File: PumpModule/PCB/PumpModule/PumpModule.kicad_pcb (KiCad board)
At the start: 2 copper layers, 55 x 105 mm, 12 parts, among them J5 Bus, J6 Motor, J7 Switch

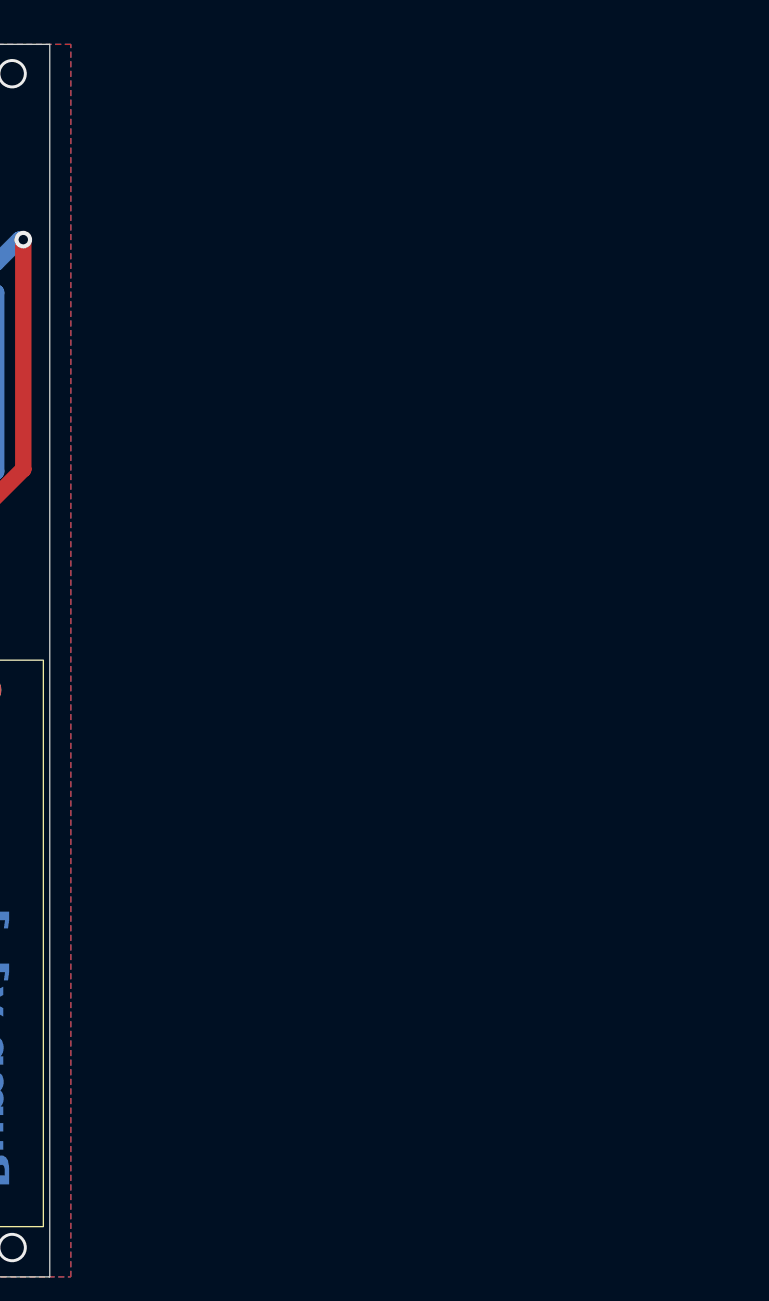
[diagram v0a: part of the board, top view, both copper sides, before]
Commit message: [PumpModule][PCB] Add Manufacturing files for 2 PumpModule v1.1 on board
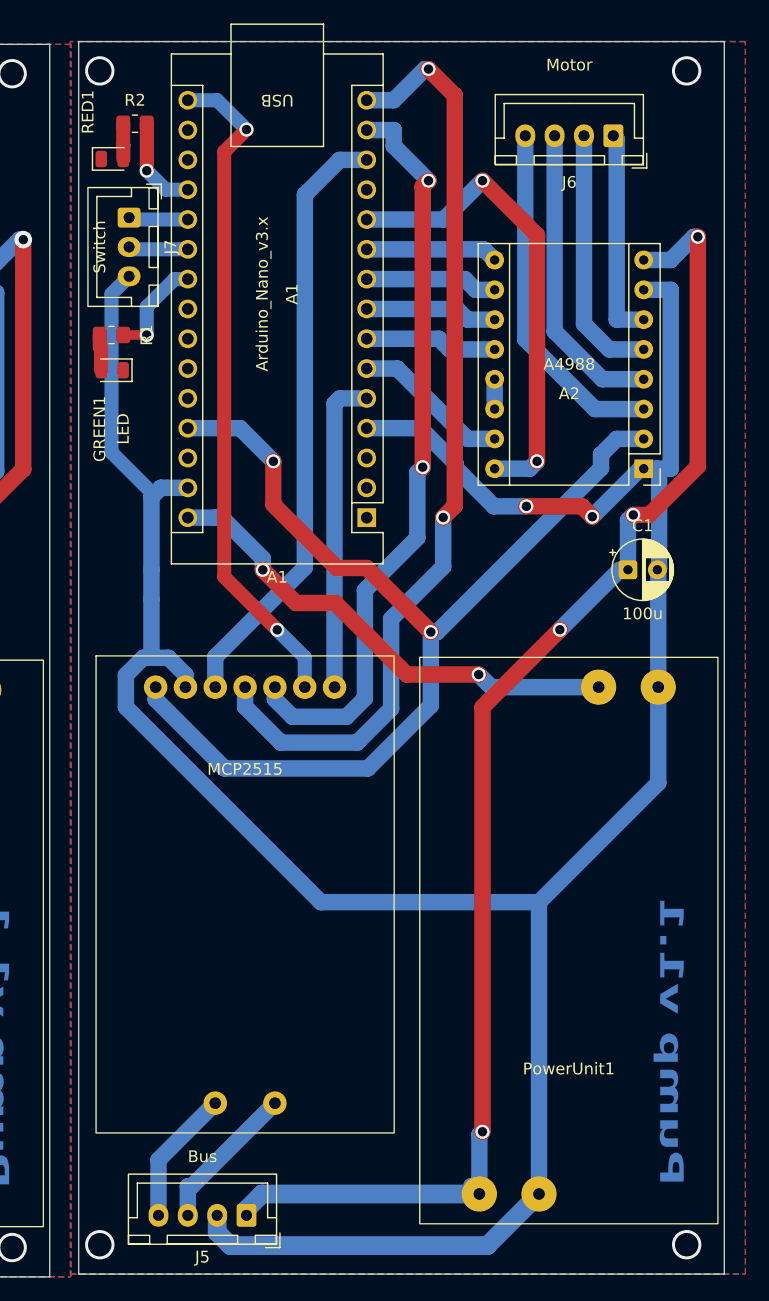
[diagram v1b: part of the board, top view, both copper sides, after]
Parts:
- added A1: Arduino_Nano_v3.x, Module:Arduino_Nano, F.Cu at (120.2, 70.3)
- added A2: A4988, Module:Pololu_Breakout-16_15.2x20.3mm, F.Cu at (143.8, 66.2)
- added C1: 100u, Capacitor_THT:CP_Radial_D5.0mm_P2.50mm, F.Cu at (142.5, 74.8)
- added GREEN1: LED, LED_SMD:LED_0805_2012Metric, F.Cu at (98.5, 57.8)
- added J5: Bus, Connector_JST:JST_XH_B4B-XH-A_1x04_P2.50mm_Vertical, F.Cu at (110.0, 129.8)
- added J6: Motor, Connector_JST:JST_XH_B4B-XH-A_1x04_P2.50mm_Vertical, F.Cu at (141.2, 37.8)
- added J7: Switch, Connector_JST:JST_XH_B3B-XH-A_1x03_P2.50mm_Vertical, F.Cu at (100.0, 44.8)
- added MCP2515: ~, PumpModule:MCP2515Mudule, F.Cu at (109.8, 92.3)
- added PowerUnit1: ~, PumpModule:DC-DC_Low, F.Cu at (137.4, 117.8)
- added R1: R, Resistor_SMD:R_0805_2012Metric_Pad1.20x1.40mm_HandSolder, F.Cu at (98.5, 54.8)
- added R2: R, Resistor_SMD:R_0805_2012Metric_Pad1.20x1.40mm_HandSolder, F.Cu at (100.5, 36.8)
- added RED1: LED, LED_SMD:LED_0805_2012Metric, F.Cu at (98.5, 39.8)
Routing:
- net GND: track 235.9 -> 471.8 mm, vias 2 -> 4
- net +12V: track 117.7 -> 235.5 mm, vias 4 -> 8
- net +5V: track 91.1 -> 182.2 mm, vias 2 -> 4
- net Net-(A1-D12): track 80.6 -> 161.2 mm, vias 2 -> 4
- net Net-(A1-D11): track 64.1 -> 128.3 mm, vias 2 -> 4
- net Net-(A1-D13): track 57.2 -> 114.3 mm, vias 2 -> 4
- net Net-(A1-D10): track 51.6 -> 103.2 mm
- net Net-(A1-VIN): track 41.5 -> 83.1 mm, vias 2 -> 4
- net Net-(A1-D8): track 40.9 -> 81.9 mm, vias 2 -> 4
- net Net-(A2-1B): track 29.9 -> 59.8 mm
- net Net-(A1-D2): track 27.1 -> 54.2 mm
- net Net-(A2-1A): track 25.9 -> 51.9 mm
- net Net-(A2-2A): track 22.0 -> 44.1 mm
- net Net-(A2-2B): track 18.1 -> 36.2 mm
- net Net-(A1-D3): track 13.4 -> 26.8 mm
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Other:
- board size 55 x 105 mm -> 112.5 x 105.2 mm

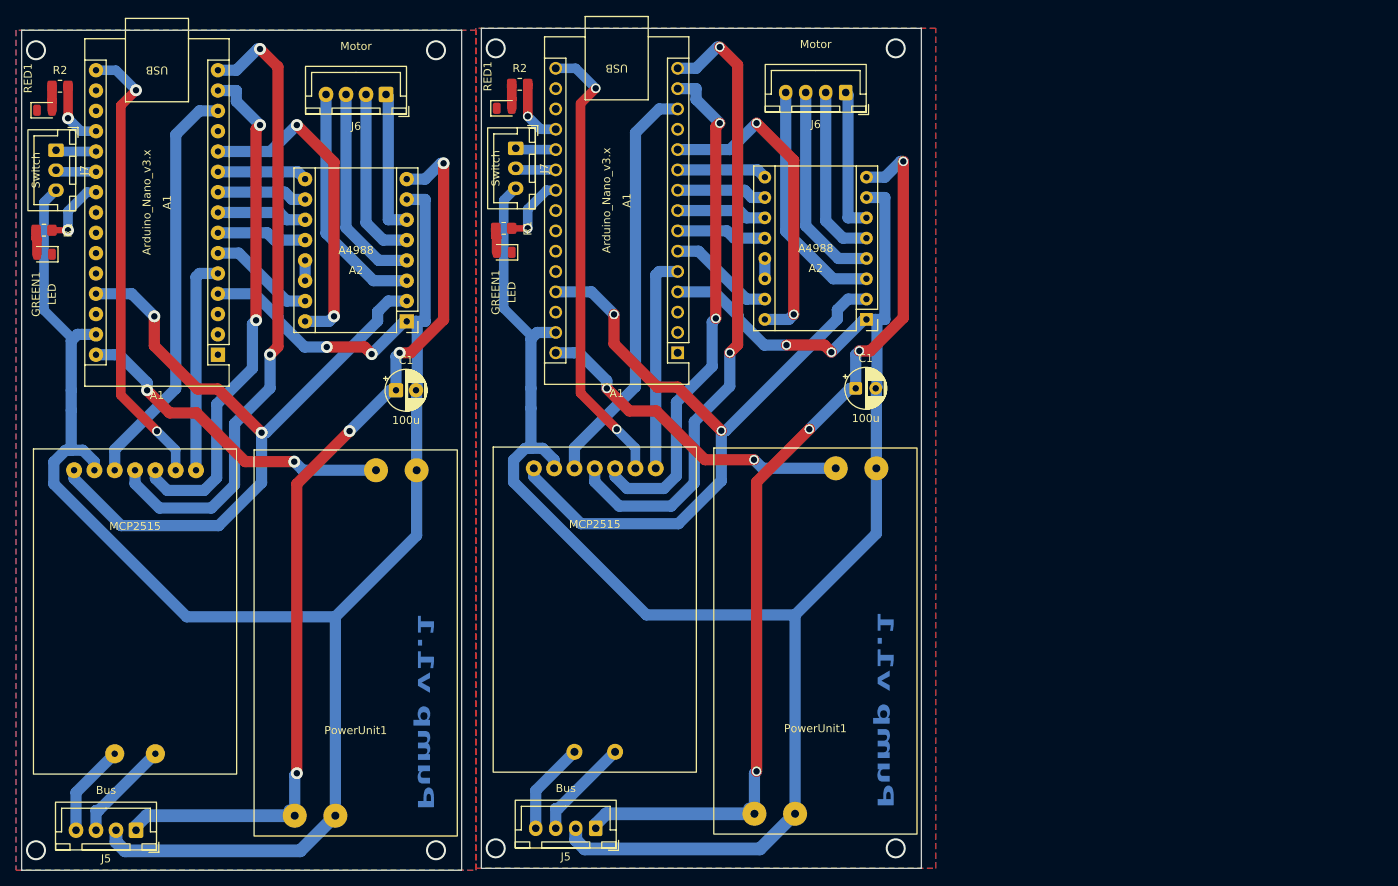
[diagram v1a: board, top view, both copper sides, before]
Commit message: [PumpModule][PCB] Fixed size of pins on PCB(v1.2)
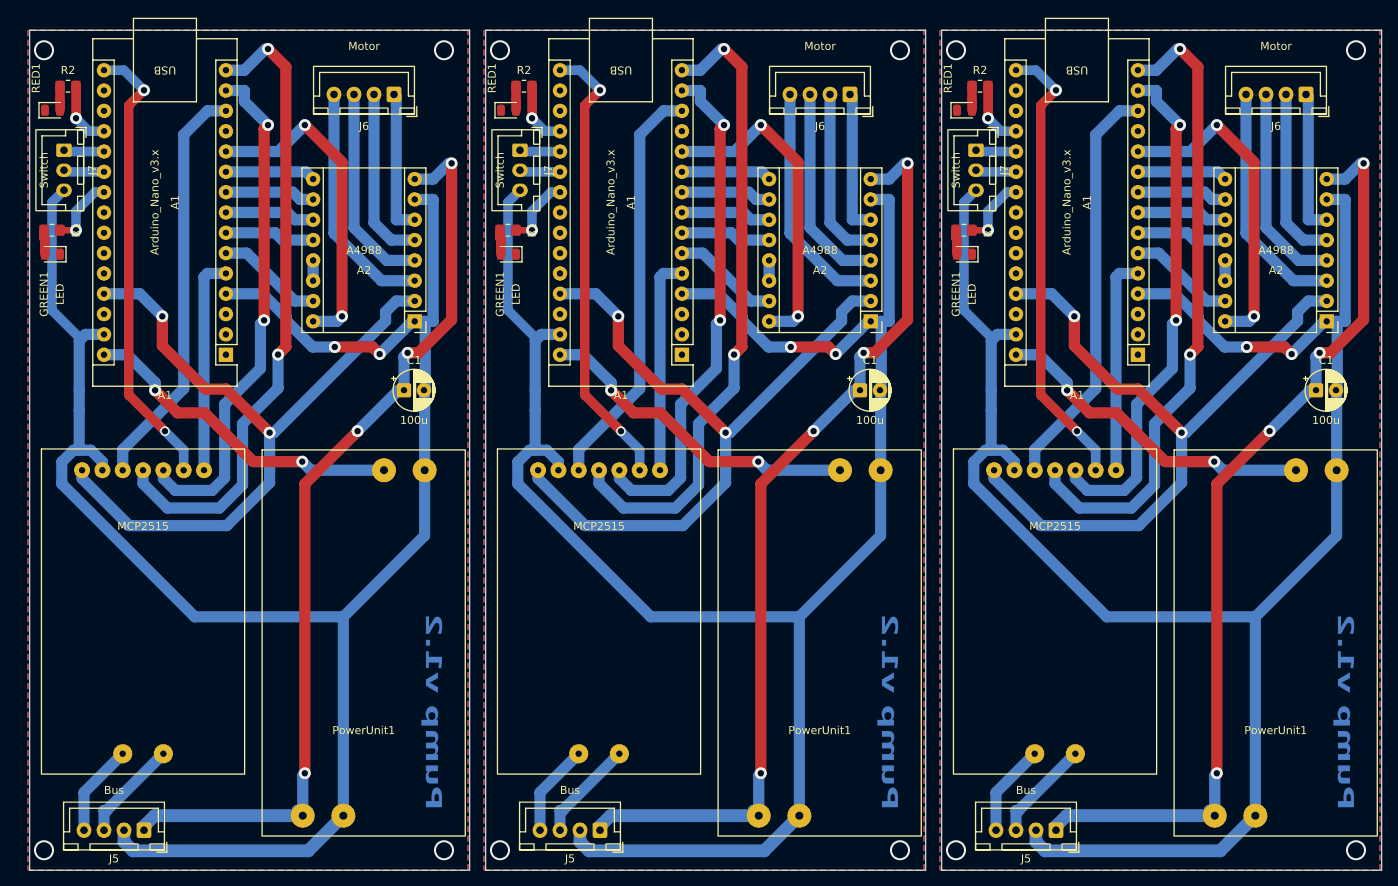
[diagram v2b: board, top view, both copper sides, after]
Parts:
- removed the A1 at (120.2, 70.3)
- removed the A2 at (143.8, 66.2)
- removed the C1 at (142.5, 74.8)
- removed the GREEN1 at (98.5, 57.8)
- removed the J5 at (110.0, 129.8)
- removed the J6 at (141.2, 37.8)
- removed the J7 at (100.0, 44.8)
- removed the MCP2515 at (109.8, 92.3)
- removed the PowerUnit1 at (137.4, 117.8)
- removed the R1 at (98.5, 54.8)
- removed the R2 at (100.5, 36.8)
- removed the RED1 at (98.5, 39.8)
- added A1: Arduino_Nano_v3.x, Module:Arduino_Nano, F.Cu at (177.7, 70.6)
- added A1: Arduino_Nano_v3.x, Module:Arduino_Nano, F.Cu at (120.7, 70.6)
- added A2: A4988, Module:Pololu_Breakout-16_15.2x20.3mm, F.Cu at (144.3, 66.4)
- added A2: A4988, Module:Pololu_Breakout-16_15.2x20.3mm, F.Cu at (201.3, 66.4)
- added C1: 100u, Capacitor_THT:CP_Radial_D5.0mm_P2.50mm, F.Cu at (200.0, 75.0)
- added C1: 100u, Capacitor_THT:CP_Radial_D5.0mm_P2.50mm, F.Cu at (143.0, 75.0)
- added GREEN1: LED, LED_SMD:LED_0805_2012Metric, F.Cu at (99.1, 58.0)
- added GREEN1: LED, LED_SMD:LED_0805_2012Metric, F.Cu at (156.1, 58.0)
- added J5: Bus, Connector_JST:JST_XH_B4B-XH-A_1x04_P2.50mm_Vertical, F.Cu at (110.5, 130.0)
- added J5: Bus, Connector_JST:JST_XH_B4B-XH-A_1x04_P2.50mm_Vertical, F.Cu at (167.5, 130.0)
- added J6: Motor, Connector_JST:JST_XH_B4B-XH-A_1x04_P2.50mm_Vertical, F.Cu at (198.8, 38.0)
- added J6: Motor, Connector_JST:JST_XH_B4B-XH-A_1x04_P2.50mm_Vertical, F.Cu at (141.8, 38.0)
- added J7: Switch, Connector_JST:JST_XH_B3B-XH-A_1x03_P2.50mm_Vertical, F.Cu at (157.5, 45.0)
- added J7: Switch, Connector_JST:JST_XH_B3B-XH-A_1x03_P2.50mm_Vertical, F.Cu at (100.5, 45.0)
- added MCP2515: ~, PumpModule:MCP2515Mudule, F.Cu at (110.4, 92.5)
- added MCP2515: ~, PumpModule:MCP2515Mudule, F.Cu at (167.4, 92.5)
- added PowerUnit1: ~, PumpModule:DC-DC_Low, F.Cu at (138.0, 118.0)
- added PowerUnit1: ~, PumpModule:DC-DC_Low, F.Cu at (195.0, 118.0)
- added R1: R, Resistor_SMD:R_0805_2012Metric_Pad1.20x1.40mm_HandSolder, F.Cu at (99.0, 55.0)
- added R1: R, Resistor_SMD:R_0805_2012Metric_Pad1.20x1.40mm_HandSolder, F.Cu at (156.0, 55.0)
- added R2: R, Resistor_SMD:R_0805_2012Metric_Pad1.20x1.40mm_HandSolder, F.Cu at (158.0, 37.0)
- added R2: R, Resistor_SMD:R_0805_2012Metric_Pad1.20x1.40mm_HandSolder, F.Cu at (101.0, 37.0)
- added RED1: LED, LED_SMD:LED_0805_2012Metric, F.Cu at (99.1, 40.0)
- added RED1: LED, LED_SMD:LED_0805_2012Metric, F.Cu at (156.1, 40.0)
- moved A1 1.00 mm to (63.7, 70.6)
- moved A2 1.00 mm to (87.3, 66.4)
- moved C1 1.00 mm to (86.0, 75.0)
- moved GREEN1 1.00 mm to (42.1, 58.0)
- moved J5 1.00 mm to (53.5, 130.0)
- moved J6 1.00 mm to (84.8, 38.0)
- moved J7 1.00 mm to (43.5, 45.0)
- moved MCP2515 1.00 mm to (53.4, 92.5)
- moved PowerUnit1 1.00 mm to (81.0, 118.0)
- moved R1 1.00 mm to (42.0, 55.0)
- moved R2 1.00 mm to (44.0, 37.0)
- moved RED1 1.00 mm to (42.1, 40.0)
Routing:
- net GND: track 471.8 -> 707.7 mm, vias 4 -> 6
- net +12V: track 235.5 -> 353.2 mm, vias 8 -> 12
- net +5V: track 182.2 -> 273.3 mm, vias 4 -> 6
- net Net-(A1-D12): track 161.2 -> 241.8 mm, vias 4 -> 6
- net Net-(A1-D11): track 128.3 -> 192.4 mm, vias 4 -> 6
- net Net-(A1-D13): track 114.3 -> 171.5 mm, vias 4 -> 6
- net Net-(A1-D10): track 103.2 -> 154.8 mm
- net Net-(A1-VIN): track 83.1 -> 124.6 mm, vias 4 -> 6
- net Net-(A1-D8): track 81.9 -> 122.8 mm, vias 4 -> 6
- net Net-(A2-1B): track 59.8 -> 89.7 mm
- net Net-(A1-D2): track 54.2 -> 81.2 mm
- net Net-(A2-1A): track 51.9 -> 77.8 mm
- net Net-(A2-2A): track 44.1 -> 66.1 mm
- net Net-(A2-2B): track 36.2 -> 54.3 mm
- net Net-(A1-D3): track 26.8 -> 40.1 mm
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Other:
- board size 112.5 x 105.2 mm -> 169 x 105 mm
- board text added: "Pump v1.2"
- board text removed: "Pump v1.1"
